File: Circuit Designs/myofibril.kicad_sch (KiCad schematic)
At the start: 66 parts

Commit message: deleted previous version files
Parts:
- C114, C115, C116, C117, C118, C119, C120, C121, C122, C123, C124, C125, C126, C127, C128, C129, C130, C131, C132, C133, C134, C135, C136, C137: renamed from C?; footprint Capacitor_SMD:C_0805_2012Metric -> CoF_Capacitor:C-0805
- C138, C139, C140, C141, C142, C143, C144, C145, C146, C147, C148, C149, C150, C151, C152, C153: renamed from C?; footprint Capacitor_SMD:C_0402_1005Metric -> CoF_Capacitor:C-0402
- R68, R69, R70, R74, R75, R76, R77, R78, R79, R80, R81, R82, R83, R84, R85, R86: renamed from R?; footprint Resistor_SMD:R_0402_1005Metric -> CoF_Resistor:R-0402
- T2: renamed from T?; footprint Resistor_SMD:R_0402_1005Metric -> CoF_Resistor:R-0402
- gave numbers to parts that had none: 9

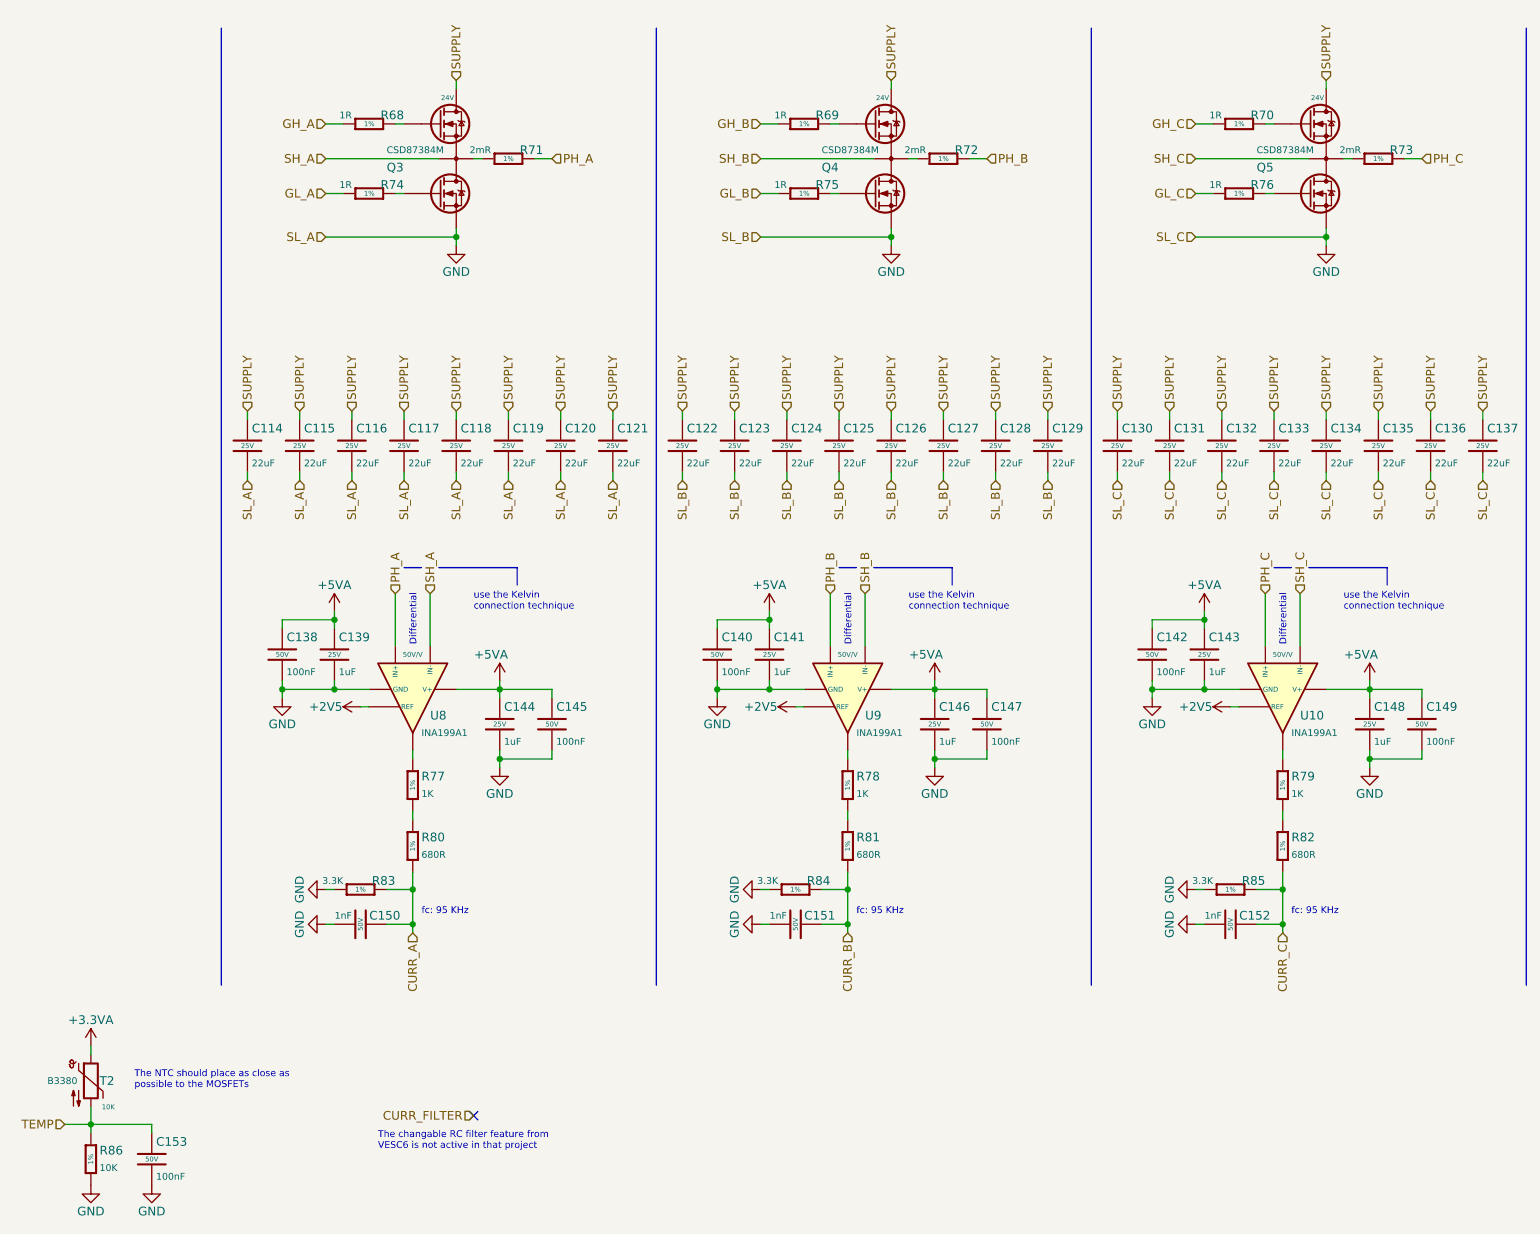
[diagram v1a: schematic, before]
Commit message: changed the LED packages, edited field reference positions
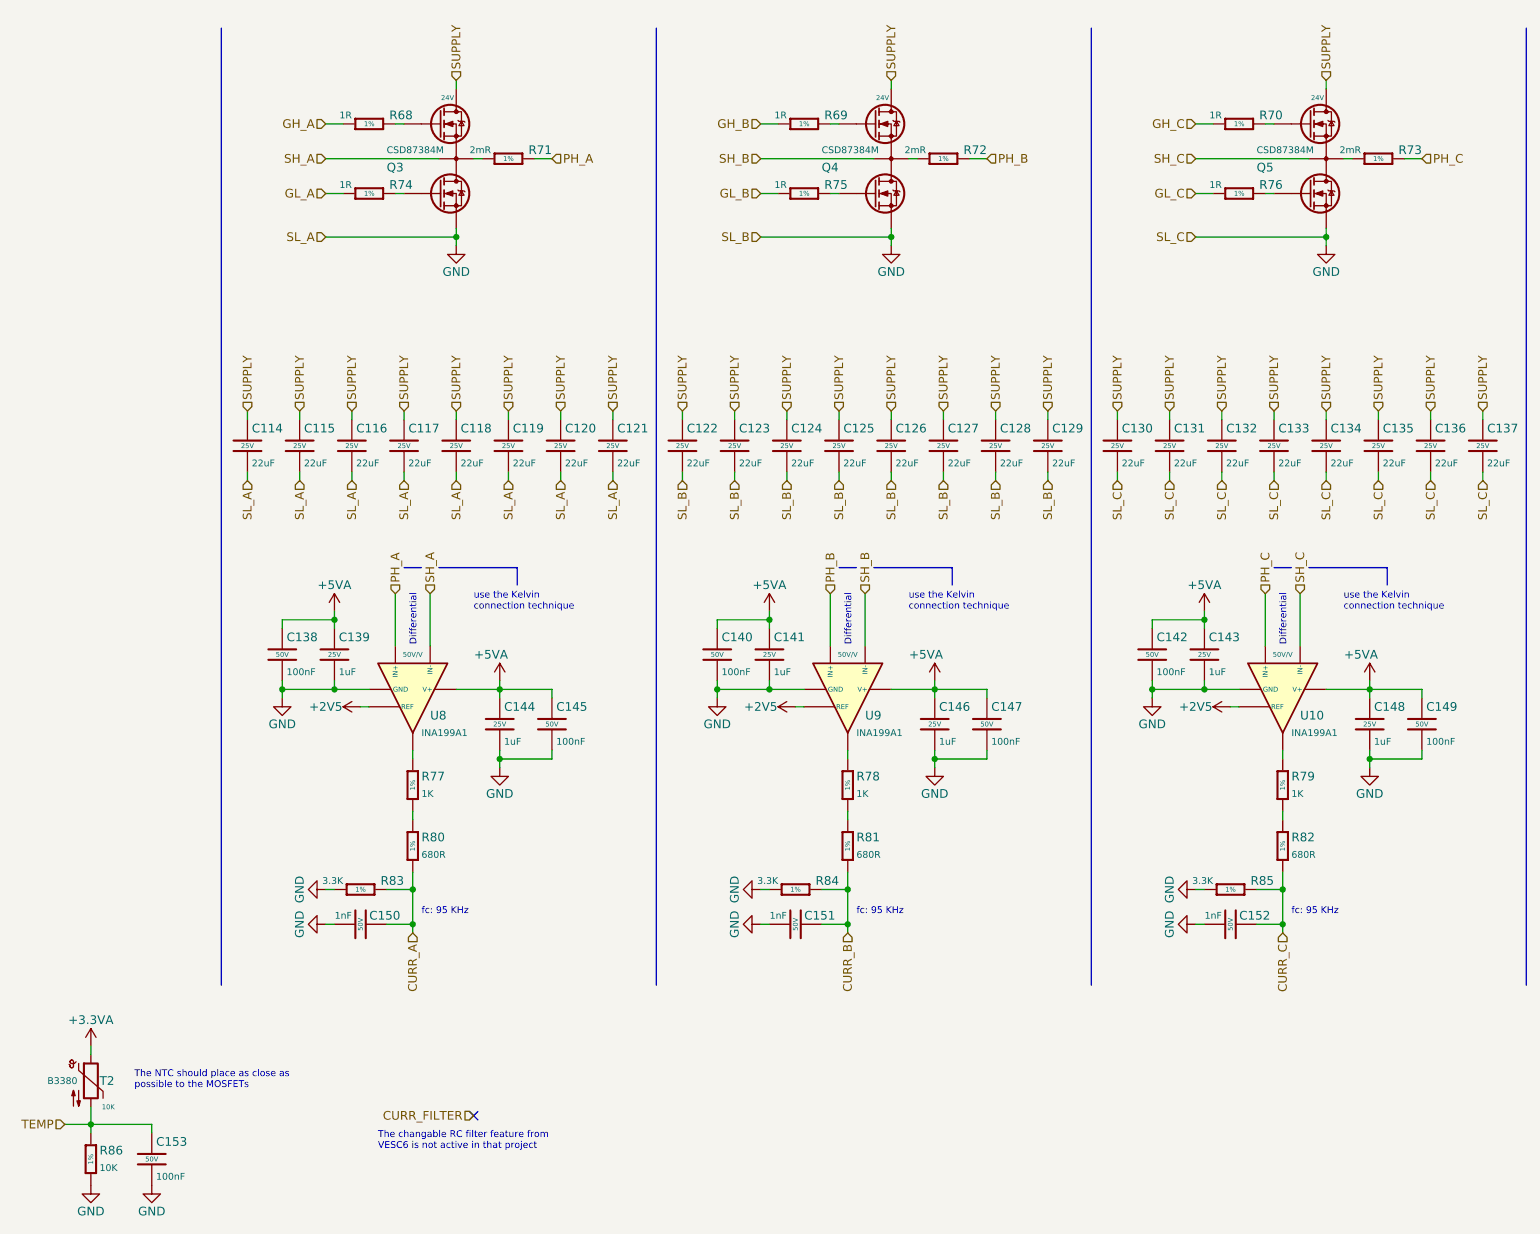
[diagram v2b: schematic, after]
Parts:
- R71, R72, R73: footprint Resistor_SMD:R_1206_3216Metric -> CoF_Resistor:R-1206
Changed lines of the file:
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@@
   (symbol (lib_id "CoE_Resistor:2mR") (at 92.71 38.1 90) (unit 1)
     (in_bom yes) (on_board yes)
-    (property "Reference" "R71" (id 0) (at 97.79 36.83 90)
+    (property "Reference" "R71" (id 0) (at 99.06 36.83 90)
       (effects (font (size 1.27 1.27)) (justify left))
     )
@@
       (effects (font (size 0.9906 0.9906)) (justify left))
     )
-    (property "Footprint" "Resistor_SMD:R_1206_3216Metric" (id 2) (at 82.55 38.1 0)
+    (property "Footprint" "CoF_Resistor:R-1206" (id 2) (at 82.55 38.1 0)
       (effects (font (size 1.27 1.27)) (justify bottom) hide)
     )
@@
   (symbol (lib_id "CoE_Resistor:1R") (at 72.39 43.18 90) (unit 1)
     (in_bom yes) (on_board yes)
-    (property "Reference" "R74" (id 0) (at 77.47 41.91 90)
+    (property "Reference" "R74" (id 0) (at 78.74 41.91 90)
       (effects (font (size 1.27 1.27)) (justify left))
     )
@@
   (symbol (lib_id "CoE_Resistor:1R") (at 72.39 33.02 90) (unit 1)
     (in_bom yes) (on_board yes)
-    (property "Reference" "R68" (id 0) (at 77.47 31.75 90)
+    (property "Reference" "R68" (id 0) (at 78.74 31.75 90)
       (effects (font (size 1.27 1.27)) (justify left))
     )
@@
   (symbol (lib_id "CoE_Resistor:1R") (at 135.89 43.18 90) (unit 1)
     (in_bom yes) (on_board yes)
-    (property "Reference" "R75" (id 0) (at 140.97 41.91 90)
+    (property "Reference" "R75" (id 0) (at 142.24 41.91 90)
       (effects (font (size 1.27 1.27)) (justify left))
     )
@@
   (symbol (lib_id "CoE_Resistor:1R") (at 135.89 33.02 90) (unit 1)
     (in_bom yes) (on_board yes)
-    (property "Reference" "R69" (id 0) (at 140.97 31.75 90)
+    (property "Reference" "R69" (id 0) (at 142.24 31.75 90)
       (effects (font (size 1.27 1.27)) (justify left))
     )
@@
   (symbol (lib_id "CoE_Resistor:2mR") (at 156.21 38.1 90) (unit 1)
     (in_bom yes) (on_board yes)
-    (property "Reference" "R72" (id 0) (at 161.29 36.83 90)
+    (property "Reference" "R72" (id 0) (at 162.56 36.83 90)
       (effects (font (size 1.27 1.27)) (justify left))
     )
@@
       (effects (font (size 0.9906 0.9906)) (justify left))
     )
-    (property "Footprint" "Resistor_SMD:R_1206_3216Metric" (id 2) (at 146.05 38.1 0)
+    (property "Footprint" "CoF_Resistor:R-1206" (id 2) (at 146.05 38.1 0)
       (effects (font (size 1.27 1.27)) (justify bottom) hide)
     )
@@
   (symbol (lib_id "CoE_Resistor:1R") (at 199.39 43.18 90) (unit 1)
     (in_bom yes) (on_board yes)
-    (property "Reference" "R76" (id 0) (at 204.47 41.91 90)
+    (property "Reference" "R76" (id 0) (at 205.74 41.91 90)
       (effects (font (size 1.27 1.27)) (justify left))
     )
@@
   (symbol (lib_id "CoE_Resistor:1R") (at 199.39 33.02 90) (unit 1)
     (in_bom yes) (on_board yes)
-    (property "Reference" "R70" (id 0) (at 204.47 31.75 90)
+    (property "Reference" "R70" (id 0) (at 205.74 31.75 90)
       (effects (font (size 1.27 1.27)) (justify left))
     )
@@
   (symbol (lib_id "CoE_Resistor:2mR") (at 219.71 38.1 90) (unit 1)
     (in_bom yes) (on_board yes)
-    (property "Reference" "R73" (id 0) (at 224.79 36.83 90)
+    (property "Reference" "R73" (id 0) (at 226.06 36.83 90)
       (effects (font (size 1.27 1.27)) (justify left))
     )
@@
       (effects (font (size 0.9906 0.9906)) (justify left))
     )
-    (property "Footprint" "Resistor_SMD:R_1206_3216Metric" (id 2) (at 209.55 38.1 0)
+    (property "Footprint" "CoF_Resistor:R-1206" (id 2) (at 209.55 38.1 0)
       (effects (font (size 1.27 1.27)) (justify bottom) hide)
     )
@@
   (symbol (lib_id "CoE_Resistor:3.3K") (at 71.12 144.78 90) (unit 1)
     (in_bom yes) (on_board yes)
-    (property "Reference" "R83" (id 0) (at 76.2 143.51 90)
+    (property "Reference" "R83" (id 0) (at 77.47 143.51 90)
       (effects (font (size 1.27 1.27)) (justify left))
     )
@@
   (symbol (lib_id "CoE_Resistor:3.3K") (at 134.62 144.78 90) (unit 1)
     (in_bom yes) (on_board yes)
-    (property "Reference" "R84" (id 0) (at 139.7 143.51 90)
+    (property "Reference" "R84" (id 0) (at 140.97 143.51 90)
       (effects (font (size 1.27 1.27)) (justify left))
     )
@@
   (symbol (lib_id "CoE_Resistor:3.3K") (at 198.12 144.78 90) (unit 1)
     (in_bom yes) (on_board yes)
-    (property "Reference" "R85" (id 0) (at 203.2 143.51 90)
-      (effects (font (size 1.27 1.27)) (justify left))
-    )
+    (property "Reference" "R85" (id 0) (at 204.47 143.51 90)
+      (effects (font (size 1.27 1.27)) (justify left))
+    )
